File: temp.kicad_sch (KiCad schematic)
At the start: 1 part, among them U2 MCP9808-E/MS

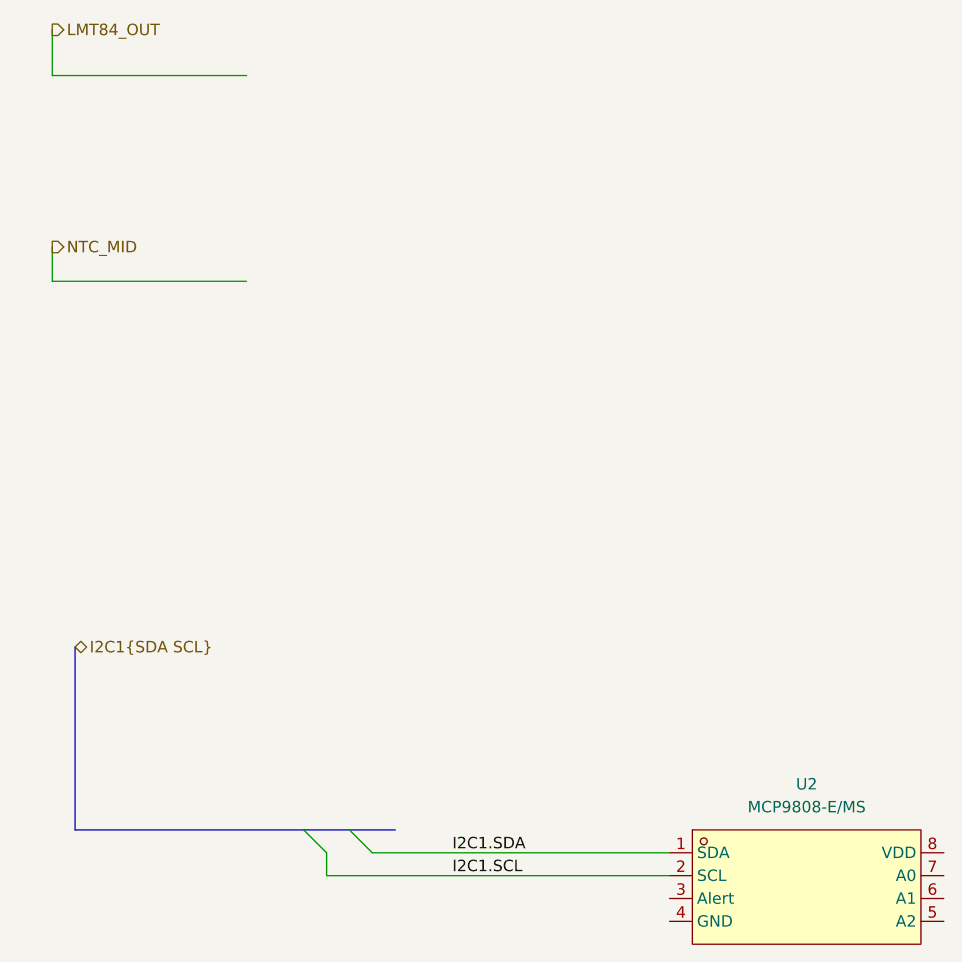
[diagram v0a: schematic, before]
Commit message: Digital, analog, and NTC temp sensors
* first

* small modifications

* change power references and cap placement

---------

Co-authored-by: Ahnaf Kamal <ahnaf.kamal@outlook.com>
Co-authored-by: alexhermeling <alex@hermeling.org>
Co-authored-by: Alex Hermeling <101155036+Alex-Hermeling@users.noreply.github.com>
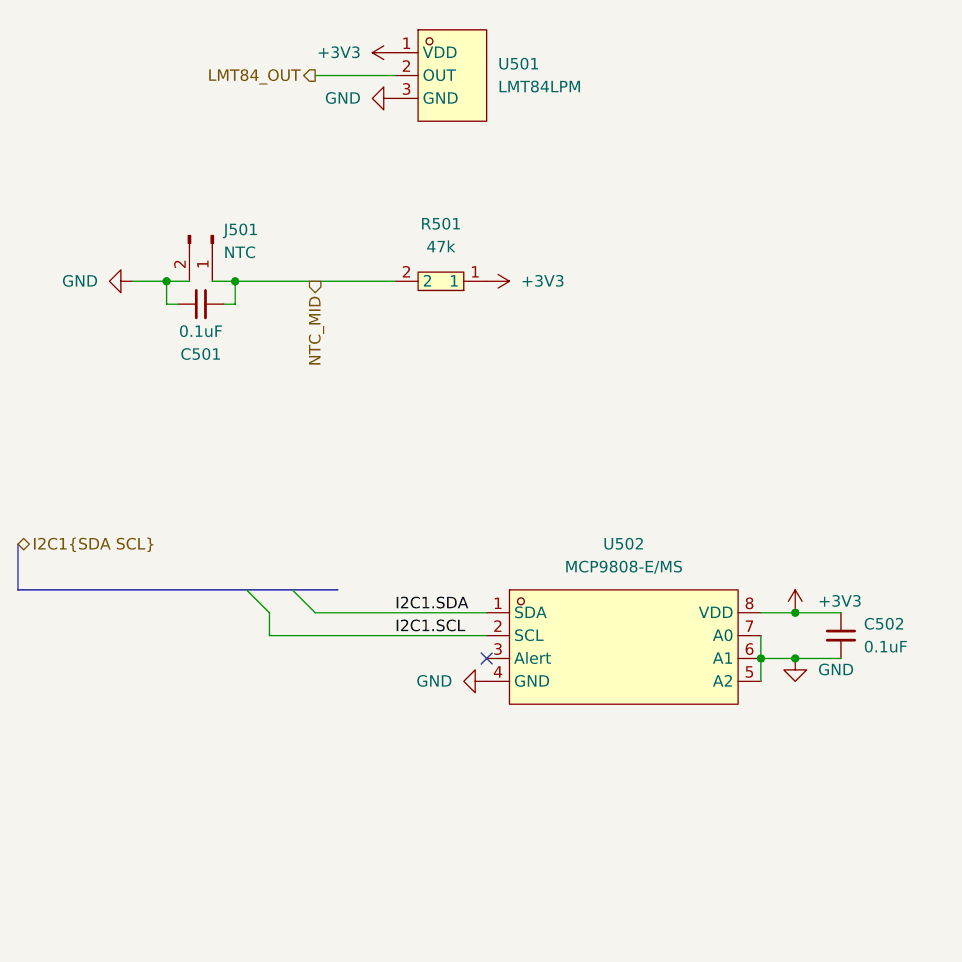
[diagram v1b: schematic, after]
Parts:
- added C501, C502: 0.1uF, EasyEDA:C0603, symbol Device:C_Small
- added J501: NTC, Package_SO:SOIC-16_3.9x9.9mm_P1.27mm, symbol Connector:Conn_01x02_Pin
- added R501: 47k, EasyEDA:R0805, symbol EasyEDA:0805W8F4702T5E
- added U501: LMT84LPM, EasyEDA:TO-92-3_L4.9-W3.7-P2.54-L, symbol EasyEDA:LMT84LPM
- renumbered U2 to U502
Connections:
- net LMT84_OUT: now also U501.2 (OUT)
- net NTC_MID: now also C501.2, J501.1 (Pin_1), R501.2
- net GND: now reaches U502.4 (GND)
- net GND: now also U502.5 (A2), U502.6 (A1), U502.7 (A0), C501.1, C502.2, J501.2 (Pin_2), U501.3 (GND)
- net +3V3: now reaches U502.8 (VDD)
- net +3V3: now also C502.1, R501.1, U501.1 (VDD)
- no-connect marks 0 -> 1
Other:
- moved on the sheet: U502
